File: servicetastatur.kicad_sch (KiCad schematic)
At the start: 70 parts, among them J1 Conn_01x02, J2 LCD, J3 Automat, J4 Tasten, J5 Conn_01x03_Pin, J6 Conn_01x03_Pin, Q1 2N3904, U1 74HC238, U17 TL7705A, U18 MC34063AP, U2 74HC00, U3 27C128, U4 80C31, U5 74LS573, U6 74HC4094, U7 74HC4094, U8 74HC165, U9 24CS16, Y1 11.059

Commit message: lcd gefixt
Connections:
- net A0: now also J2.5 (Pin_5); no longer J2.12 (Pin_12)
- net A1: now also J2.4 (Pin_4); no longer J2.13 (Pin_13)
- net D0: now also J2.7 (Pin_7); no longer J2.10 (Pin_10)
- net D1: now also J2.8 (Pin_8); no longer J2.9 (Pin_9)
- net D2: now also J2.9 (Pin_9); no longer J2.8 (Pin_8)
- net D3: now also J2.10 (Pin_10); no longer J2.7 (Pin_7)
- net D4: now also J2.11 (Pin_11); no longer J2.6 (Pin_6)
- net D5: now also J2.12 (Pin_12); no longer J2.5 (Pin_5)
- net D6: now also J2.13 (Pin_13); no longer J2.4 (Pin_4)
- net D7: now also J2.14 (Pin_14); no longer J2.3 (Pin_3)
- net GND: no longer J2.2 (Pin_2), R1.1, R2.2
- net VCC: now also J2.2 (Pin_2), R1.1, R2.2
- net Kontrast: now reaches R1.2
- net Kontrast: now also J2.3 (Pin_3); no longer J2.14 (Pin_14)
- net LCD_EN: now reaches U1.7 (Y7)
- net LCD_EN: now also J2.6 (Pin_6); no longer J2.11 (Pin_11)
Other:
- moved on the sheet: C9, J2

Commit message: kompakt
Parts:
- removed C11, C19: C, Capacitor_THT:CP_Radial_Tantal_D4.5mm_P2.50mm, symbol Device:C
- removed C12: C_Polarized, Capacitor_THT:CP_Radial_D5.0mm_P2.00mm, symbol Device:C_Polarized
- removed C7: C, Capacitor_THT:C_Axial_L3.8mm_D2.6mm_P7.50mm_Horizontal, symbol Device:C
- removed D1: 1N5819, adp:D_DO-15_P15mm_Horizontal, symbol Device:D
- removed D2: D, Diode_THT:D_DO-15_P15.24mm_Horizontal, symbol Device:D
- removed J1: Conn_01x02, Connector_Wire:SolderWire-0.5sqmm_1x02_P4.8mm_D0.9mm_OD2.3mm, symbol Connector_Generic:Conn_01x02
- removed J2: LCD, adp:FFC_2x08_P1mm_Vertical, symbol Connector_Generic:Conn_02x08_Odd_Even
- removed J4: Tasten, adp:FFC_1x06_P2.50mm_Horizontal, symbol Connector:Conn_01x06_Socket
- removed J5, J6: Conn_01x03_Pin, Connector_PinSocket_2.54mm:PinSocket_1x03_P2.54mm_Vertical, symbol Connector:Conn_01x03_Pin
- removed Q1: 2N3904, adp:TO-92, symbol Transistor_BJT:2N3904
- removed R12, R2: 22 Ω, Resistor_THT:R_Axial_DIN0207_L6.3mm_D2.5mm_P10.16mm_Horizontal, symbol Device:R
- removed R13: 47 kΩ, Resistor_THT:R_Axial_DIN0207_L6.3mm_D2.5mm_P10.16mm_Horizontal, symbol Device:R
- removed R15: 1 kΩ, Resistor_THT:R_Axial_DIN0207_L6.3mm_D2.5mm_P10.16mm_Horizontal, symbol Device:R
- removed R19, R5: 270 Ω, Resistor_THT:R_Axial_DIN0207_L6.3mm_D2.5mm_P10.16mm_Horizontal, symbol Device:R
- removed R20, R21, R22: 1 Ω, Resistor_THT:R_Axial_DIN0207_L6.3mm_D2.5mm_P10.16mm_Horizontal, symbol Device:R
- removed R23: 100 Ω, Resistor_THT:R_Axial_DIN0207_L6.3mm_D2.5mm_P10.16mm_Horizontal, symbol Device:R
- removed R24: 100 kΩ, Resistor_THT:R_Axial_DIN0207_L6.3mm_D2.5mm_P10.16mm_Horizontal, symbol Device:R
- removed R4: 3.3 kΩ, Resistor_THT:R_Axial_DIN0207_L6.3mm_D2.5mm_P10.16mm_Horizontal, symbol Device:R
- removed R6: 220 Ω, Resistor_THT:R_Axial_DIN0414_L11.9mm_D4.5mm_P15.24mm_Horizontal, symbol Device:R
- removed U1: 74HC238, Package_DIP:DIP-16_W7.62mm, symbol 74xx:74HC238
- removed U18: MC34063AP, Package_DIP:DIP-8_W7.62mm, symbol Regulator_Switching:MC34063AP
- removed U4: 80C31, Package_LCC:PLCC-44_THT-Socket, symbol MCU_Atmel:TS80C31
- removed U5: 74LS573, Package_DIP:DIP-20_W7.62mm, symbol 74xx:74LS573
- removed U6, U7: 74HC4094, Package_DIP:DIP-16_W7.62mm, symbol MCU_Atmel:74HC4094
- removed U8: 74HC165, Package_DIP:DIP-16_W7.62mm, symbol 74xx:74HC165
- removed U9: 24CS16, Package_DIP:DIP-8_W7.62mm, symbol Memory_EEPROM:24LC16
- added D1: LED, LED_SMD:LED_0603_1608Metric, symbol Device:LED
- added F1: Fuse, Fuse:Fuse_0805_2012Metric, symbol Device:Fuse
- added J2: Conn_02x08_Odd_Even_MountingPin, ConnPad:LCDdisplay, symbol Connector_Generic_MountingPin:Conn_02x08_Odd_Even_MountingPin
- added RV1: Kontrast, Potentiometer_THT:Potentiometer_ACP_CA9-V10_Vertical_Hole, symbol Device:R_Potentiometer
- added RV2: Helligkeit, Potentiometer_THT:Potentiometer_ACP_CA9-V10_Vertical_Hole, symbol Device:R_Potentiometer
- added SW1: OK, Button_Switch_THT:SW_PUSH_6mm, symbol Switch:SW_Push
- added SW2: →, Button_Switch_THT:SW_PUSH_6mm, symbol Switch:SW_Push
- added SW3: F3, Button_Switch_THT:SW_PUSH_6mm, symbol Switch:SW_Push
- added SW4: F4, Button_Switch_THT:SW_PUSH_6mm, symbol Switch:SW_Push
- added SW5: ←, Button_Switch_THT:SW_PUSH_6mm, symbol Switch:SW_Push
- added SW6: F1, Button_Switch_THT:SW_PUSH_6mm, symbol Switch:SW_Push
- added SW7: ↑, Button_Switch_THT:SW_PUSH_6mm, symbol Switch:SW_Push
- added SW8: ↓, Button_Switch_THT:SW_PUSH_6mm, symbol Switch:SW_Push
- added SW9: F2, Button_Switch_THT:SW_PUSH_6mm, symbol Switch:SW_Push
- added U1: ~, Package_DIP:DIP-40_W15.24mm, symbol MCU_Atmel:TS80C31_DIP
- added U11: 80C31, Package_LCC:PLCC-44_THT-Socket, symbol MCU_Atmel:TS80C31_PLCC
- added U12: 74LS573, Package_SO:SOIC-20W_7.5x12.8mm_P1.27mm, symbol 74xx:74LS573
- added U13: 74HC165, Package_SO:SOIC-16W_5.3x10.2mm_P1.27mm, symbol 74xx:74HC165
- added U15: 24CS16, Package_SO:SO-8_3.9x4.9mm_P1.27mm, symbol Memory_EEPROM:24LC16
- added U16: 74HC238, Package_SO:SOIC-16W_5.3x10.2mm_P1.27mm, symbol 74xx:74HC238
- added U19, U20: 74HC4094, Package_SO:SOIC-16W_5.3x10.2mm_P1.27mm, symbol MCU_Atmel:74HC4094
- added Y2: 11.059, Crystal:Crystal_SMD_HC49-SD, symbol Device:Crystal
- C1: value C_Polarized -> 1uF; footprint Capacitor_THT:CP_Radial_D5.0mm_P2.50mm -> Capacitor_SMD:C_1206_3216Metric
- C10: value C -> 0,1uF; footprint Capacitor_THT:CP_Radial_Tantal_D4.5mm_P2.50mm -> Capacitor_SMD:C_0603_1608Metric
- C13, C14, C15, C16, C17, C18, C22, C5: value C -> 100nF; footprint Capacitor_THT:C_Axial_L3.8mm_D2.6mm_P7.50mm_Horizontal -> Capacitor_SMD:C_0603_1608Metric
- C2: value C_Polarized -> 1uF; footprint Capacitor_THT:CP_Radial_D5.0mm_P2.00mm -> Capacitor_SMD:C_1206_3216Metric
- C20, C21: value C -> 100nF; footprint Capacitor_THT:CP_Radial_Tantal_D4.5mm_P2.50mm -> Capacitor_SMD:C_0603_1608Metric
- C3: footprint Capacitor_THT:C_Axial_L3.8mm_D2.6mm_P7.50mm_Horizontal -> Capacitor_SMD:C_0603_1608Metric
- C4: value C -> 1uF; footprint Capacitor_THT:C_Axial_L3.8mm_D2.6mm_P7.50mm_Horizontal -> Capacitor_SMD:C_0603_1608Metric
- C6: value C -> 0,1uF; footprint Capacitor_THT:C_Axial_L3.8mm_D2.6mm_P7.50mm_Horizontal -> Capacitor_SMD:C_0603_1608Metric
- C8, C9: value C -> 33pF; footprint Capacitor_THT:CP_Radial_Tantal_D4.5mm_P2.50mm -> Capacitor_SMD:C_0603_1608Metric
- D3: footprint Diode_THT:D_DO-15_P15.24mm_Horizontal -> Diode_SMD:D_2010_5025Metric
- D4: footprint Diode_THT:D_A-405_P7.62mm_Horizontal -> Diode_SMD:D_0805_2012Metric
- R1: value 3.3 kΩ -> 470; footprint Resistor_THT:R_Axial_DIN0207_L6.3mm_D2.5mm_P10.16mm_Horizontal -> Resistor_SMD:R_0603_1608Metric
- R10, R11, R14, R16, R17, R18, R25, R3, R7, R8, R9: footprint Resistor_THT:R_Axial_DIN0207_L6.3mm_D2.5mm_P10.16mm_Horizontal -> Resistor_SMD:R_0603_1608Metric
- U17: footprint Package_DIP:DIP-8_W7.62mm -> Package_SO:SO-8_3.9x4.9mm_P1.27mm
- U2: footprint Package_DIP:DIP-14_W7.62mm -> Package_SO:SOIC-14_3.9x8.7mm_P1.27mm
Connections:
- net +VDC: now also F1.1
- net A0: now also J2.5 (Pin_5), U12.12 (Q7)
- net A1: now also J2.4 (Pin_4), U12.13 (Q6)
- net A14: now also U1.27 (P2.6/A14), U11.30 (P2.6/A14), U16.4 (~{E1})
- net A15: now also R25.2, U1.28 (P2.7/A15), U11.31 (P2.7/A15), U11.34 (NIC), U16.5 (~{E2})
- net A2: now also U12.14 (Q5)
- net A3: now also U12.15 (Q4)
- net A4: now also U12.16 (Q3), U16.1 (A0)
- net A5: now also U12.17 (Q2), U16.2 (A1)
- net A6: now also U12.18 (Q1), U16.3 (A2)
- net A7: now also U12.19 (Q0)
- net ALE: now also U1.30 (ALE), U11.33 (ALE), U12.11 (Load)
- net CLOCK: now also U13.2 (CP), U19.3 (CP), U20.3 (CP)
- net D0: now also J2.7 (Pin_7), U1.39 (P0.0/AD0), U11.43 (P0.0/AD0), U12.9 (D7), U13.11 (D0), U19.11 (QP7), U20.11 (QP7)
- net D1: now also J2.8 (Pin_8), U1.38 (P0.1/AD1), U11.42 (P0.1/AD1), U12.8 (D6), U13.12 (D1), U19.14 (QP4), U20.12 (QP6)
- net D2: now also J2.9 (Pin_9), U1.37 (P0.2/AD2), U11.41 (P0.2/AD2), U12.7 (D5), U13.13 (D2), U19.13 (QP5), U20.13 (QP5)
- net D3: now also J2.10 (Pin_10), U1.36 (P0.3/AD3), U11.40 (P0.3/AD3), U12.6 (D4), U13.14 (D3), U19.12 (QP6), U20.14 (QP4)
- net D4: now also J2.11 (Pin_11), U1.35 (P.04/AD4), U11.39 (P.04/AD4), U12.5 (D3), U13.3 (D4), U19.7 (QP3), U20.7 (QP3)
- net D5: now also J2.12 (Pin_12), U1.34 (P0.5/AD5), U11.38 (P0.5/AD5), U12.4 (D2), U13.4 (D5), U19.6 (QP2), U20.6 (QP2)
- net D6: now also J2.13 (Pin_13), U1.33 (P0.6/AD6), U11.37 (P0.6/AD6), U12.3 (D1), U13.5 (D6), U19.5 (QP1), U20.5 (QP1)
- net D7: now also J2.14 (Pin_14), U1.32 (P0.7/AD7), U11.36 (P0.7/AD7), U12.2 (D0), U13.6 (D7), U19.4 (QP0), U20.4 (QP0)
- net GND: now also R1.1, R11.1, J2.1 (Pin_1), J2.16 (Pin_16), J2.MP (MountPin), U1.20 (Vss), U1.31 (~{EA}/Vpp), U11.1 (Vss1), U11.22 (Vss), U11.35 (EA), U12.1 (OE), U12.10 (GND), U13.8 (GND), U15.1 (A0), U15.2 (A1), U15.3 (A2), U15.4 (GND), U15.7 (WP), U16.8 (GND), U19.8 (GND), U20.8 (GND)
- net Kontrast: now also J2.3 (Pin_3), RV1.2, RV1.3; no longer R1.2
- net LCD_EN: now also J2.6 (Pin_6), U16.7 (Y7)
- net RESET: now also R11.2, U17.6 (RESET), U1.9 (RST), U11.10 (RST)
- net SCL: now also U1.15 (P3.5/T1), U11.17 (P3.5/T1), U15.6 (SCL)
- net SDA: now also U1.14 (P3.4/T0), U11.16 (P3.4/T0), U15.5 (SDA)
- net VCC: now also U17.2 (~{RESIN}), D1.2 (A), F1.2, J2.2 (Pin_2), RV1.1, RV2.1, U1.40 (Vcc), U11.44 (Vcc), U12.20 (VCC), U13.16 (VCC), U15.8 (VCC), U16.16 (VCC), U19.16 (VCC), U20.16 (VCC); no longer R1.1, R11.2
- net at C3.1, D4.1 (K), R3.1: now also U19.1 (STR), U20.1 (STR)
- net at U2.4, U2.5: now also U16.9 (Y6)
- net at U2.6: now also U13.1 (~{PL})
- net at U2.11: now also U1.12 (P3.2/INT0), U11.14 (P3.2/INT0)
- net at U2.12, U2.13, U2.3: now also U1.13 (P3.3/INT1), U11.15 (P3.3/INT1)
- net at U2.10: now also U1.16 (P3.6/WR), U11.18 (P3.6/WR)
- net at U2.9: now also U1.17 (P3.7/RD), U11.19 (P3.7/RD)
- net at C8.2, Y1.2: now also U1.18 (XTAL2), U11.20 (XTAL2), Y2.2
- net at C9.2, Y1.1: now also U1.19 (XTAL1), U11.21 (XTAL1), Y2.1
- net at U3.25 (A8): now also U1.21 (P2.0/A8), U11.24 (P2.0/A8)
- net at U3.24 (A9): now also U1.22 (P2.1/A9), U11.25 (P2.1/A9)
- net at U3.21 (A10): now also U1.23 (P2.2/A10), U11.26 (P2.2/A10)
- net at U3.23 (A11): now also U1.24 (P2.3/A11), U11.27 (P2.3/A11)
- net at U3.2 (A12): now also U1.25 (P2.4/A12), U11.28 (P2.4/A12)
- net at U3.26 (A13): now also U1.26 (P2.5/A13), U11.29 (P2.5/A13)
- net at U3.20 (~{CE}), U3.22 (~{OE}): now also U1.29 (PSEN), U11.32 (PSEN)
- net at R18.1: now also U20.2 (D)
- net at U2.8: now also U16.6 (E3)
- net at R14.1: now also U13.10 (DS), U13.15 (~{CE})
- net at R16.1: now also U13.9 (Q7)
- new net: SW3.1, SW6.1, SW9.1, U1.3 (P1.2), U11.4 (P1.2)
- new net: SW7.2, SW8.2, SW9.2, U1.7 (P1.6), U11.8 (P1.6)
- new net: D1.1 (K), R1.2
- new net: SW1.1, SW4.1, SW7.1, U1.1 (P1.0), U11.2 (P1.0)
- new net: SW4.2, SW5.2, SW6.2, U1.6 (P1.5), U11.7 (P1.5)
- new net: U1.10 (P3.0/RxD), U11.11 (P3.0/RxD)
- new net: U1.11 (P3.1/TxD), U11.13 (P3.1/TxD)
- new net: SW2.1, SW5.1, SW8.1, U1.2 (P1.1), U11.3 (P1.1)
- new net: U1.4 (P1.3), U11.5 (P1.3)
- new net: SW1.2, SW2.2, SW3.2, U1.5 (P1.4), U11.6 (P1.4)
- new net: U1.8 (P1.7), U11.9 (P1.7)
- new net: U16.10 (Y5), U19.15 (OE)
- new net: U16.11 (Y4), U20.15 (OE)
- new net: U19.2 (D), U20.9 (QS1)
- new net Helligkeit: J2.15 (Pin_15), RV2.2, RV2.3
- no-connect marks 15 -> 13
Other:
- moved on the sheet: C10, C6, R11, U17

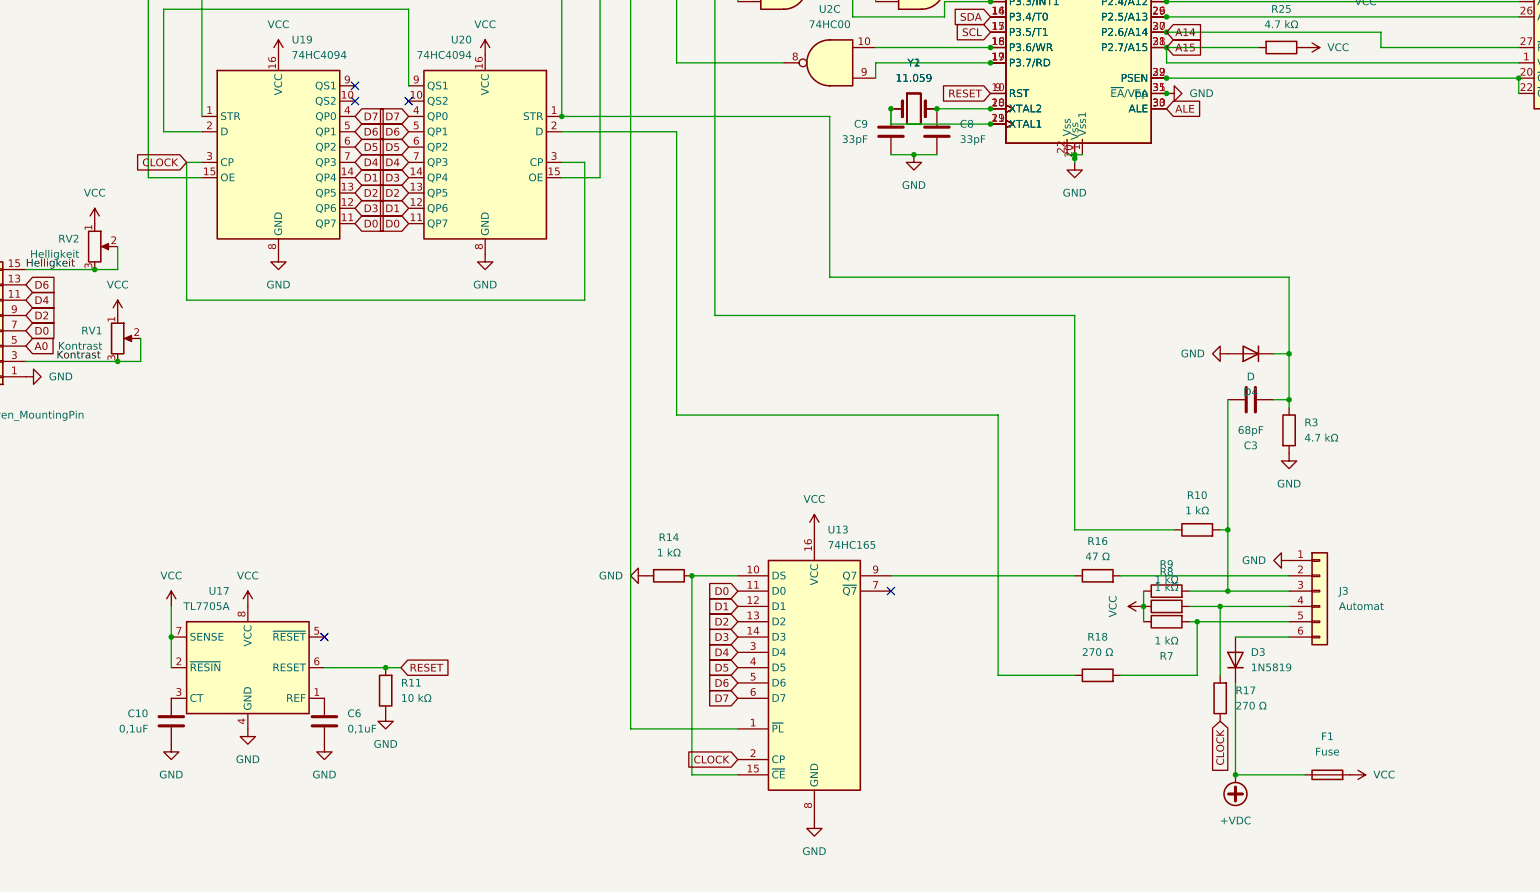
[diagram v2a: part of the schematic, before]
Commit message: replace reset circuit with cap
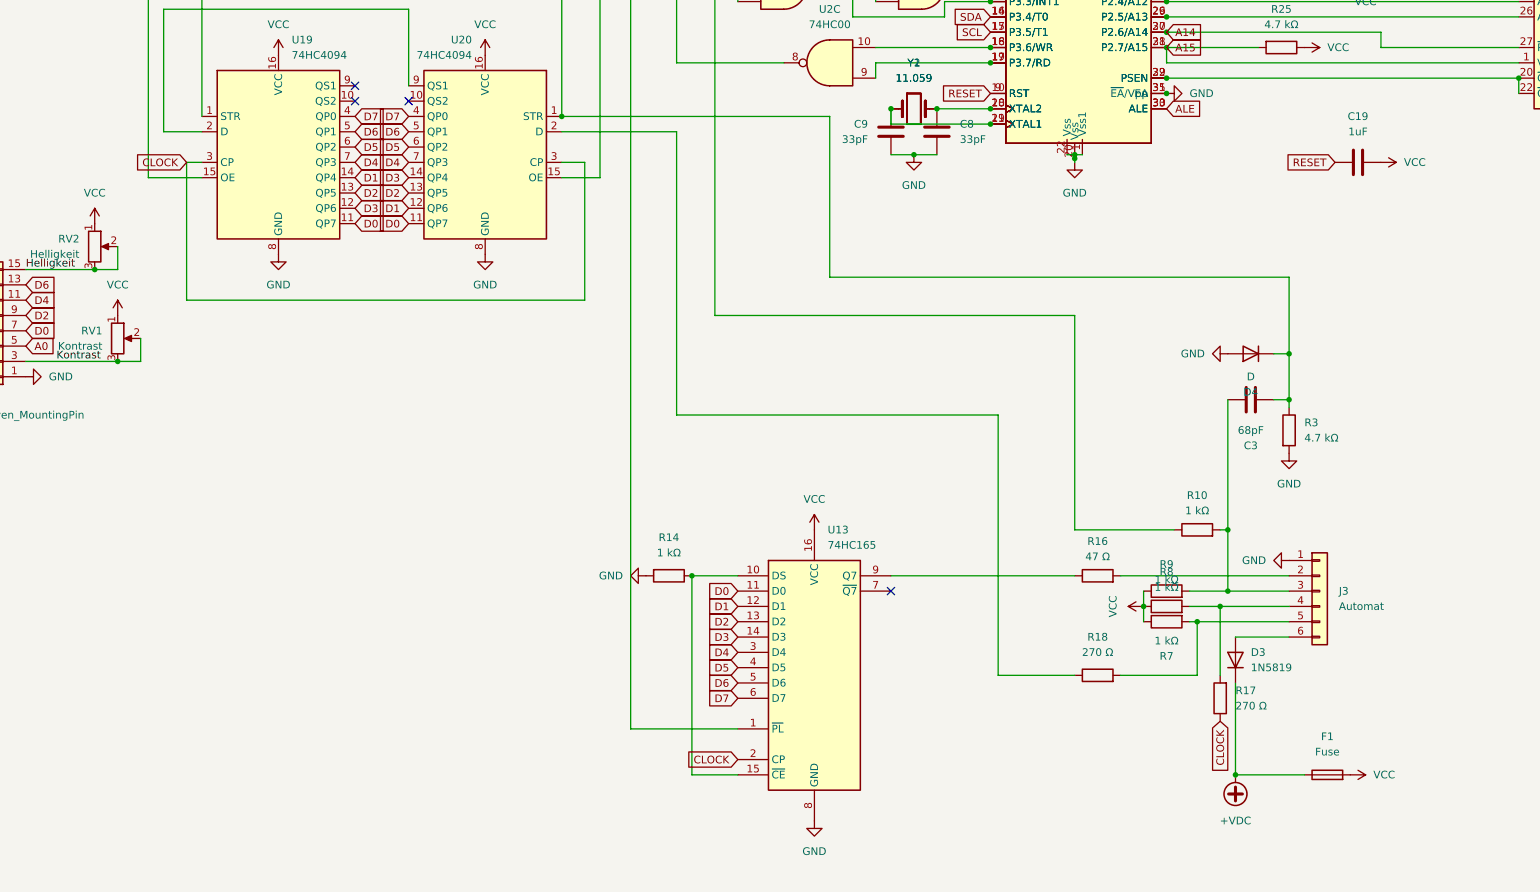
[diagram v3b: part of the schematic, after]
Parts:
- removed C10, C6: 0,1uF, Capacitor_SMD:C_0603_1608Metric, symbol Device:C
- removed R11: 10 kΩ, Resistor_SMD:R_0603_1608Metric, symbol Device:R
- removed U17: TL7705A, Package_SO:SO-8_3.9x4.9mm_P1.27mm, symbol Power_Supervisor:TL7705A
- added C19: 1uF, Capacitor_SMD:C_0603_1608Metric, symbol Device:C
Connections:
- net RESET: now also C19.1
- net VCC: now also C19.2
- no-connect marks 13 -> 12

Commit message: bestellt 2
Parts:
- removed C3: 68pF, Capacitor_SMD:C_0603_1608Metric, symbol Device:C
- added C10, C11, C12: 33pF, Capacitor_SMD:C_0603_1608Metric, symbol Device:C
- added H1, H2: MountingHole_Pad_MP, MountingHole:MountingHole_3.7mm_Pad, symbol Mechanical:MountingHole_Pad_MP
- C9: now not fitted; now left out of the parts list
- D3: footprint Diode_SMD:D_2010_5025Metric -> Diode_SMD:D_SOD-123
- D4: value D -> 1N5819; footprint Diode_SMD:D_0805_2012Metric -> Diode_SMD:D_SOD-123
- F1: value Fuse -> 0,5A
- J3: now left out of the parts list
- RV1: value Kontrast -> 10k; footprint Potentiometer_THT:Potentiometer_ACP_CA9-V10_Vertical_Hole -> Potentiometer_THT:Potentiometer_Piher_PT-10-V10_Vertical_Hole
- RV2: value Helligkeit -> 10k; footprint Potentiometer_THT:Potentiometer_ACP_CA9-V10_Vertical_Hole -> Potentiometer_THT:Potentiometer_Piher_PT-10-V10_Vertical_Hole
- U1: value ~ -> DIP-40 Socket
- U11: value 80C31 -> PLCC-44_THT-Socket
- U12: value 74LS573 -> 74HC573; footprint Package_SO:SOIC-20W_7.5x12.8mm_P1.27mm -> Package_SO:TSSOP-20_4.4x6.5mm_P0.65mm
- U13: footprint Package_SO:SOIC-16W_5.3x10.2mm_P1.27mm -> Package_SO:SOP-16_4.4x10.4mm_P1.27mm
- U3: value 27C128 -> DIP-28 Socket
- Y1: footprint Crystal:Resonator-2Pin_W7.0mm_H2.5mm -> Crystal:Crystal_HC49-U_Vertical; now not fitted; now left out of the parts list
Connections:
- net GND: now also C10.1, C11.1, H1.MP, H2.MP
- net at D4.1 (K), R3.1, U19.1 (STR)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: now also C12.1
- net at J3.3 (Pin_3), R10.2, R9.2: now also C12.2
- net at C8.2, U1.18 (XTAL2), U11.20 (XTAL2)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: now also C11.2
- net at C9.2, U1.19 (XTAL1), U11.21 (XTAL1)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: now also C10.2

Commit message: kontrast gnd
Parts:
- RV1, RV2: footprint Potentiometer_THT:Potentiometer_Piher_PT-10-V10_Vertical_Hole -> Potentiometer_THT:Potentiometer_ACP_CA9-V10_Vertical_Hole
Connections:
- net GND: now also RV1.1
- net VCC: no longer RV1.1
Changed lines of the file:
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@@
+	)
+	(symbol
+		(lib_id "power:GND")
+		(at 55.88 118.11 180)
+		(unit 1)
+		(exclude_from_sim no)
+		(in_bom yes)
+		(on_board yes)
+		(dnp no)
+		(fields_autoplaced yes)
+		(property "Reference" "#PWR063"
+			(at 55.88 111.76 0)
+			(effects
+				(font
+					(size 1.27 1.27)
+				)
+				(hide yes)
+			)
+		)
+		(property "Value" "GND"
+			(at 55.88 113.03 0)
+			(effects
+				(font
+					(size 1.27 1.27)
+				)
+			)
+		)
+		(property "Footprint" ""
+			(at 55.88 118.11 0)
+			(effects
+				(font
+					(size 1.27 1.27)
+				)
+				(hide yes)
+			)
+		)
+		(property "Datasheet" ""
+			(at 55.88 118.11 0)
+			(effects
+				(font
+					(size 1.27 1.27)
+				)
+				(hide yes)
+			)
+		)
+		(property "Description" "Power symbol creates a global label with name \"GND\" , ground"
+			(at 55.88 118.11 0)
+			(effects
+				(font
+					(size 1.27 1.27)
+				)
+				(hide yes)
+			)
+		)
+		(pin "1"
+		)
+		(instances
+			(project "servicetastatur"
+				(path "/f1547e98-e012-47b0-8f5e-c4ff3a098fc5"
+					(reference "#PWR063")
+					(unit 1)
+				)
+			)
+		)
 	)
 	(symbol
@@
 			)
 		)
-		(property "Footprint" "Potentiometer_THT:Potentiometer_Piher_PT-10-V10_Vertical_Hole"
+		(property "Footprint" "Potentiometer_THT:Potentiometer_ACP_CA9-V10_Vertical_Hole"
 			(at 55.88 121.92 0)
 			(effects
@@
 	)
 	(symbol
-		(lib_id "power:VCC")
-		(at 55.88 118.11 0)
-		(unit 1)
-		(exclude_from_sim no)
-		(in_bom yes)
-		(on_board yes)
-		(dnp no)
-		(fields_autoplaced yes)
-		(property "Reference" "#PWR078"
-			(at 55.88 121.92 0)
-			(effects
-				(font
-					(size 1.27 1.27)
-				)
-				(hide yes)
-			)
-		)
-		(property "Value" "VCC"
-			(at 55.88 113.03 0)
-			(effects
-				(font
-					(size 1.27 1.27)
-				)
-			)
-		)
-		(property "Footprint" ""
-			(at 55.88 118.11 0)
-			(effects
-				(font
-					(size 1.27 1.27)
-				)
-				(hide yes)
-			)
-		)
-		(property "Datasheet" ""
-			(at 55.88 118.11 0)
-			(effects
-				(font
-					(size 1.27 1.27)
-				)
-				(hide yes)
-			)
-		)
-		(property "Description" "Power symbol creates a global label with name \"VCC\""
-			(at 55.88 118.11 0)
-			(effects
-				(font
-					(size 1.27 1.27)
-				)
-				(hide yes)
-			)
-		)
-		(pin "1"
-		)
-		(instances
-			(project "servicetastatur"
-				(path "/f1547e98-e012-47b0-8f5e-c4ff3a098fc5"
-					(reference "#PWR078")
-					(unit 1)
-				)
-			)
-		)
-	)
-	(symbol
 		(lib_id "power:GND")
 		(at 250.19 158.75 270)
@@
 			)
 		)
-		(property "Footprint" "Potentiometer_THT:Potentiometer_Piher_PT-10-V10_Vertical_Hole"
+		(property "Footprint" "Potentiometer_THT:Potentiometer_ACP_CA9-V10_Vertical_Hole"
 			(at 52.07 106.68 0)
 			(effects
